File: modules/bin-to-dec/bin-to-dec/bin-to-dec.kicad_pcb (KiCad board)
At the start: 2 copper layers, 78 parts, among them J1 Conn_02x26_Odd_Even, Q100 2N7002, Q101 2N7002, Q102 DMP3099L, Q103 DMP3099L, Q104 2N7002, Q105 2N7002, Q106 2N7002, Q107 DMP3099L, Q108 DMP3099L, Q109 DMP3099L, Q110 DMP3099L, Q111 2N7002, Q112 2N7002, Q113 2N7002, Q114 2N7002, Q115 DMP3099L, Q116 DMP3099L, Q117 DMP3099L, Q118 2N7002, Q119 2N7002, Q120 DMP3099L, Q121 DMP3099L, Q122 2N7002, Q123 2N7002, Q124 2N7002, Q125 DMP3099L, Q126 DMP3099L, Q127 DMP3099L, Q128 2N7002, Q129 2N7002, Q130 2N7002, Q131 DMP3099L, Q132 DMP3099L, Q133 DMP3099L, Q134 2N7002, Q135 2N7002, Q136 DMP3099L, Q137 DMP3099L, Q138 2N7002, Q139 2N7002, Q140 2N7002, Q141 DMP3099L, Q142 DMP3099L, Q143 DMP3099L, Q144 2N7002, Q145 2N7002, Q146 2N7002, Q147 DMP3099L, Q148 DMP3099L, Q75 DMP3099L, Q76 2N7002, Q77 2N7002, Q78 2N7002, Q79 DMP3099L, Q80 DMP3099L, Q81 DMP3099L, Q82 2N7002, Q83 2N7002, Q84 2N7002, Q85 DMP3099L, Q86 DMP3099L, Q87 DMP3099L, Q88 2N7002, Q89 2N7002, Q90 2N7002, Q91 DMP3099L, Q92 DMP3099L, Q93 DMP3099L, Q94 2N7002, Q95 2N7002, Q96 2N7002, Q97 DMP3099L, Q98 DMP3099L, Q99 DMP3099L

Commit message: routed on bdc
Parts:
- added C1: 100n, Capacitor_SMD:C_0603_1608Metric, F.Cu at (250.4, -17.8)
- added C2: 100n, Capacitor_SMD:C_0603_1608Metric, F.Cu at (250.4, -15.3)
- added C3: 100n, Capacitor_SMD:C_0603_1608Metric, F.Cu at (250.4, -12.8)
- added Q1: DMP3099L, Package_TO_SOT_SMD:SOT-23, F.Cu at (253.6, 31.8)
- added Q10: DMP3099L, Package_TO_SOT_SMD:SOT-23, F.Cu at (238.6, -3.65)
- added Q11: DMP3099L, Package_TO_SOT_SMD:SOT-23, F.Cu at (242.8, 31.9)
- added Q12: 2N7002, Package_TO_SOT_SMD:SOT-23, F.Cu at (238.3, 31.9)
- added Q13: 2N7002, Package_TO_SOT_SMD:SOT-23, F.Cu at (238.3, 27.9)
- added Q14: 2N7002, Package_TO_SOT_SMD:SOT-23, F.Cu at (238.3, 35.6)
- added Q15: DMP3099L, Package_TO_SOT_SMD:SOT-23, F.Cu at (242.8, 27.9)
- added Q16: DMP3099L, Package_TO_SOT_SMD:SOT-23, F.Cu at (242.8, 35.6)
- added Q17: DMP3099L, Package_TO_SOT_SMD:SOT-23, F.Cu at (242.6, 18.9)
- added Q18: 2N7002, Package_TO_SOT_SMD:SOT-23, F.Cu at (238.2, 18.9)
- added Q19: 2N7002, Package_TO_SOT_SMD:SOT-23, F.Cu at (238.1, 14.9)
- added Q2: 2N7002, Package_TO_SOT_SMD:SOT-23, F.Cu at (249.1, 31.8)
- added Q20: 2N7002, Package_TO_SOT_SMD:SOT-23, F.Cu at (238.2, 22.6)
- added Q21: DMP3099L, Package_TO_SOT_SMD:SOT-23, F.Cu at (242.6, 14.9)
- added Q22: DMP3099L, Package_TO_SOT_SMD:SOT-23, F.Cu at (242.6, 22.6)
- added Q23: DMP3099L, Package_TO_SOT_SMD:SOT-23, F.Cu at (234.2, -7.83)
- added Q24: 2N7002, Package_TO_SOT_SMD:SOT-23, F.Cu at (234.2, -3.62)
- added Q25: 2N7002, Package_TO_SOT_SMD:SOT-23, F.Cu at (230.4, -7.79)
- added Q26: DMP3099L, Package_TO_SOT_SMD:SOT-23, F.Cu at (230.4, -3.65)
- added Q27: DMP3099L, Package_TO_SOT_SMD:SOT-23, F.Cu at (232.6, 19.0)
- added Q28: 2N7002, Package_TO_SOT_SMD:SOT-23, F.Cu at (228.1, 19.0)
- added Q29: 2N7002, Package_TO_SOT_SMD:SOT-23, F.Cu at (228.1, 15.0)
- added Q3: 2N7002, Package_TO_SOT_SMD:SOT-23, F.Cu at (249.1, 27.9)
- added Q30: 2N7002, Package_TO_SOT_SMD:SOT-23, F.Cu at (228.1, 22.8)
- added Q31: DMP3099L, Package_TO_SOT_SMD:SOT-23, F.Cu at (232.6, 15.0)
- added Q32: DMP3099L, Package_TO_SOT_SMD:SOT-23, F.Cu at (232.6, 22.8)
- added Q33: DMP3099L, Package_TO_SOT_SMD:SOT-23, F.Cu at (232.5, 6.17)
- added Q34: 2N7002, Package_TO_SOT_SMD:SOT-23, F.Cu at (228.0, 6.17)
- added Q35: 2N7002, Package_TO_SOT_SMD:SOT-23, F.Cu at (228.0, 2.20)
- added Q36: 2N7002, Package_TO_SOT_SMD:SOT-23, F.Cu at (228.0, 9.95)
- added Q37: DMP3099L, Package_TO_SOT_SMD:SOT-23, F.Cu at (232.5, 2.20)
- added Q38: DMP3099L, Package_TO_SOT_SMD:SOT-23, F.Cu at (232.5, 9.95)
- added Q39: DMP3099L, Package_TO_SOT_SMD:SOT-23, F.Cu at (241.7, -13.1)
- added Q4: 2N7002, Package_TO_SOT_SMD:SOT-23, F.Cu at (249.2, 35.6)
- added Q40: DMP3099L, Package_TO_SOT_SMD:SOT-23, F.Cu at (245.5, -13.0)
- added Q41: 2N7002, Package_TO_SOT_SMD:SOT-23, F.Cu at (241.7, -17.4)
- added Q42: 2N7002, Package_TO_SOT_SMD:SOT-23, F.Cu at (245.5, -17.4)
- added Q43: 2N7002, Package_TO_SOT_SMD:SOT-23, F.Cu at (237.6, -17.4)
- added Q44: 2N7002, Package_TO_SOT_SMD:SOT-23, F.Cu at (233.6, -17.4)
- added Q45: DMP3099L, Package_TO_SOT_SMD:SOT-23, F.Cu at (237.6, -13.1)
- added Q46: DMP3099L, Package_TO_SOT_SMD:SOT-23, F.Cu at (233.6, -13.1)
- added Q47: DMP3099L, Package_TO_SOT_SMD:SOT-23, F.Cu at (253.5, 18.9)
- added Q48: 2N7002, Package_TO_SOT_SMD:SOT-23, F.Cu at (249.0, 18.9)
- added Q49: 2N7002, Package_TO_SOT_SMD:SOT-23, F.Cu at (249.0, 15.0)
- added Q5: DMP3099L, Package_TO_SOT_SMD:SOT-23, F.Cu at (253.6, 27.9)
- added Q50: 2N7002, Package_TO_SOT_SMD:SOT-23, F.Cu at (249.0, 22.7)
- added Q51: DMP3099L, Package_TO_SOT_SMD:SOT-23, F.Cu at (253.4, 15.0)
- added Q52: DMP3099L, Package_TO_SOT_SMD:SOT-23, F.Cu at (253.5, 22.7)
- added Q53: DMP3099L, Package_TO_SOT_SMD:SOT-23, F.Cu at (253.4, 6.08)
- added Q54: 2N7002, Package_TO_SOT_SMD:SOT-23, F.Cu at (248.9, 6.08)
- added Q55: 2N7002, Package_TO_SOT_SMD:SOT-23, F.Cu at (248.9, 2.10)
- added Q56: 2N7002, Package_TO_SOT_SMD:SOT-23, F.Cu at (248.9, 9.85)
- added Q57: DMP3099L, Package_TO_SOT_SMD:SOT-23, F.Cu at (253.4, 2.10)
- added Q58: DMP3099L, Package_TO_SOT_SMD:SOT-23, F.Cu at (253.4, 9.85)
- added Q59: DMP3099L, Package_TO_SOT_SMD:SOT-23, F.Cu at (250.6, -7.84)
- added Q6: DMP3099L, Package_TO_SOT_SMD:SOT-23, F.Cu at (253.6, 35.6)
- added Q60: 2N7002, Package_TO_SOT_SMD:SOT-23, F.Cu at (250.6, -3.63)
- added Q61: 2N7002, Package_TO_SOT_SMD:SOT-23, F.Cu at (246.7, -7.81)
- added Q62: DMP3099L, Package_TO_SOT_SMD:SOT-23, F.Cu at (246.7, -3.66)
- added Q63: DMP3099L, Package_TO_SOT_SMD:SOT-23, F.Cu at (232.7, 31.8)
- added Q64: 2N7002, Package_TO_SOT_SMD:SOT-23, F.Cu at (228.2, 31.8)
- added Q65: 2N7002, Package_TO_SOT_SMD:SOT-23, F.Cu at (228.2, 27.9)
- added Q66: 2N7002, Package_TO_SOT_SMD:SOT-23, F.Cu at (228.2, 35.6)
- added Q67: DMP3099L, Package_TO_SOT_SMD:SOT-23, F.Cu at (232.6, 27.9)
- added Q68: DMP3099L, Package_TO_SOT_SMD:SOT-23, F.Cu at (232.7, 35.6)
- added Q69: DMP3099L, Package_TO_SOT_SMD:SOT-23, F.Cu at (242.5, 6.03)
- added Q7: DMP3099L, Package_TO_SOT_SMD:SOT-23, F.Cu at (242.4, -7.83)
- added Q70: 2N7002, Package_TO_SOT_SMD:SOT-23, F.Cu at (238.1, 6.03)
- added Q71: 2N7002, Package_TO_SOT_SMD:SOT-23, F.Cu at (238.0, 2.05)
- added Q72: 2N7002, Package_TO_SOT_SMD:SOT-23, F.Cu at (238.1, 9.80)
- added Q73: DMP3099L, Package_TO_SOT_SMD:SOT-23, F.Cu at (242.5, 2.05)
- added Q74: DMP3099L, Package_TO_SOT_SMD:SOT-23, F.Cu at (242.5, 9.80)
- added Q8: 2N7002, Package_TO_SOT_SMD:SOT-23, F.Cu at (242.4, -3.62)
- added Q9: 2N7002, Package_TO_SOT_SMD:SOT-23, F.Cu at (238.6, -7.79)
- moved J1 269.1 mm to (301.3, -48.1)
- moved Q110 164.9 mm to (208.4, -14.6), turned to -90 degrees
- moved Q112 163.4 mm to (208.4, -18.9), turned to -90 degrees
- moved Q109 159.2 mm to (204.6, -14.6), turned to -90 degrees
- moved Q111 157.7 mm to (204.6, -18.9), turned to -90 degrees
- moved Q113 150.6 mm to (200.5, -18.9), turned to -90 degrees
- moved Q114 150.4 mm to (196.5, -18.9), turned to -90 degrees
- moved Q115 144.0 mm to (200.5, -14.6), turned to -90 degrees
- moved Q116 143.8 mm to (196.5, -14.6), turned to -90 degrees
- moved Q131 123.1 mm to (217.4, 2.07)
- moved Q132 121.4 mm to (217.4, 9.82)
- moved Q129 114.7 mm to (212.9, 2.07)
- moved Q130 113.2 mm to (212.9, 9.82)
- moved Q141 113.1 mm to (206.3, 14.9)
- moved Q127 113.1 mm to (217.4, 6.04)
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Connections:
- J1 pad 1: unconnected-(J1-Pin_1-Pad1) -> +3V3
- J1 pad 10: unconnected-(J1-Pin_10-Pad10) -> /BDC1/8
- J1 pad 11: unconnected-(J1-Pin_11-Pad11) -> +3V3
- J1 pad 12: unconnected-(J1-Pin_12-Pad12) -> GND
- J1 pad 13: unconnected-(J1-Pin_13-Pad13) -> /BDC/\Q1
- J1 pad 14: unconnected-(J1-Pin_14-Pad14) -> /BDC1/7
- J1 pad 15: unconnected-(J1-Pin_15-Pad15) -> /BDC/Q1
- J1 pad 16: unconnected-(J1-Pin_16-Pad16) -> /BDC1/6
- J1 pad 17: unconnected-(J1-Pin_17-Pad17) -> /BDC/\Q0
- J1 pad 18: unconnected-(J1-Pin_18-Pad18) -> /BDC1/5
- J1 pad 19: unconnected-(J1-Pin_19-Pad19) -> /BDC/Q0
- J1 pad 2: unconnected-(J1-Pin_2-Pad2) -> GND
- J1 pad 20: unconnected-(J1-Pin_20-Pad20) -> /BDC1/4
- J1 pad 21: unconnected-(J1-Pin_21-Pad21) -> +3V3
- J1 pad 22: unconnected-(J1-Pin_22-Pad22) -> GND
- J1 pad 23: unconnected-(J1-Pin_23-Pad23) -> /BDC/0
- J1 pad 24: unconnected-(J1-Pin_24-Pad24) -> /BDC1/3
- J1 pad 25: unconnected-(J1-Pin_25-Pad25) -> /BDC/1
- J1 pad 26: unconnected-(J1-Pin_26-Pad26) -> /BDC1/2
- J1 pad 27: unconnected-(J1-Pin_27-Pad27) -> /BDC/2
- J1 pad 28: unconnected-(J1-Pin_28-Pad28) -> /BDC1/1
- J1 pad 29: unconnected-(J1-Pin_29-Pad29) -> /BDC/3
- J1 pad 3: unconnected-(J1-Pin_3-Pad3) -> /BDC/\Q3
- J1 pad 30: unconnected-(J1-Pin_30-Pad30) -> /BDC1/0
- J1 pad 31: unconnected-(J1-Pin_31-Pad31) -> +3V3
- J1 pad 32: unconnected-(J1-Pin_32-Pad32) -> GND
- J1 pad 33: unconnected-(J1-Pin_33-Pad33) -> /BDC/4
- J1 pad 34: unconnected-(J1-Pin_34-Pad34) -> /BDC1/Q0
- J1 pad 35: unconnected-(J1-Pin_35-Pad35) -> /BDC/5
- J1 pad 36: unconnected-(J1-Pin_36-Pad36) -> /BDC1/\Q0
- J1 pad 37: unconnected-(J1-Pin_37-Pad37) -> /BDC/6
- J1 pad 38: unconnected-(J1-Pin_38-Pad38) -> /BDC1/Q1
- J1 pad 39: unconnected-(J1-Pin_39-Pad39) -> /BDC/7
- J1 pad 40: unconnected-(J1-Pin_40-Pad40) -> /BDC1/\Q1
- J1 pad 41: unconnected-(J1-Pin_41-Pad41) -> +3V3
- J1 pad 42: unconnected-(J1-Pin_42-Pad42) -> GND
- J1 pad 43: unconnected-(J1-Pin_43-Pad43) -> /BDC/8
- J1 pad 44: unconnected-(J1-Pin_44-Pad44) -> /BDC1/Q2
- J1 pad 45: unconnected-(J1-Pin_45-Pad45) -> /BDC/9
- J1 pad 46: unconnected-(J1-Pin_46-Pad46) -> /BDC1/\Q2
- J1 pad 47: unconnected-(J1-Pin_47-Pad47) -> +3V3
- J1 pad 48: unconnected-(J1-Pin_48-Pad48) -> /BDC1/Q3
- J1 pad 5: unconnected-(J1-Pin_5-Pad5) -> /BDC/Q3
- J1 pad 50: unconnected-(J1-Pin_50-Pad50) -> /BDC1/\Q3
- J1 pad 52: unconnected-(J1-Pin_52-Pad52) -> GND
- J1 pad 6: unconnected-(J1-Pin_6-Pad6) -> GND
- J1 pad 7: unconnected-(J1-Pin_7-Pad7) -> /BDC/\Q2
- J1 pad 8: unconnected-(J1-Pin_8-Pad8) -> /BDC1/9
- J1 pad 9: unconnected-(J1-Pin_9-Pad9) -> /BDC/Q2
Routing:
- net /BDC1/\Q1: track 0.00 -> 135.0 mm, vias 0 -> 9
- net /BDC1/Q0: track 0.00 -> 114.0 mm, vias 0 -> 10
- net +3V3: track 0.00 -> 112.3 mm, vias 0 -> 74
- net /BDC1/\Q0: track 0.00 -> 107.5 mm, vias 0 -> 10
- net /BDC1/Q1: track 0.00 -> 103.2 mm, vias 0 -> 7
- net /BDC1/5: track 0.00 -> 101.0 mm, vias 0 -> 2
- net /BDC1/6: track 0.00 -> 77.0 mm
- net /BDC1/nand5/Out: track 0.00 -> 75.3 mm, vias 0 -> 5
- net /BDC1/\Q2: track 0.00 -> 71.3 mm, vias 0 -> 3
- net /BDC1/9: track 0.00 -> 69.3 mm
- net /BDC1/4: track 0.00 -> 68.6 mm
- net /BDC1/\Q3: track 0.00 -> 63.3 mm, vias 0 -> 3
- net /BDC1/Q3: track 0.00 -> 63.3 mm, vias 0 -> 1
- net /BDC1/nand1/Out: track 0.00 -> 61.2 mm, vias 0 -> 4
- net /BDC1/8: track 0.00 -> 55.9 mm
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
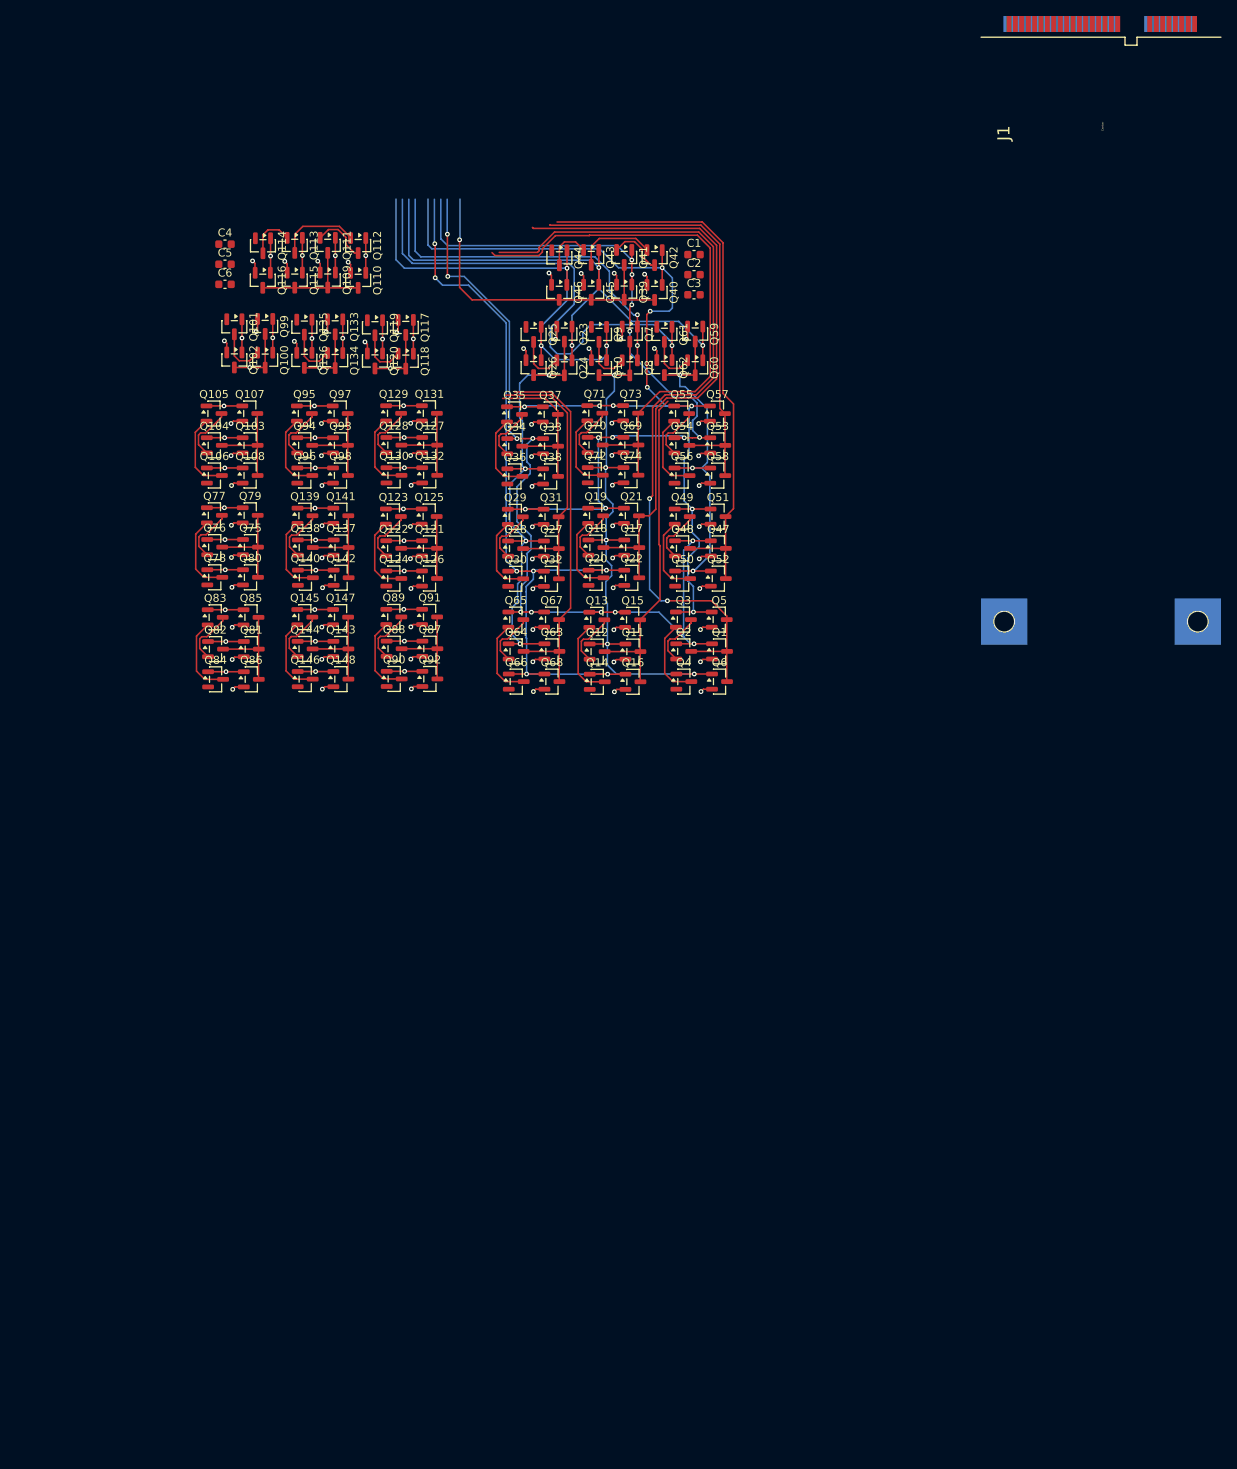
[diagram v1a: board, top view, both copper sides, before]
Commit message: went from routed bin-to-dec to gate only
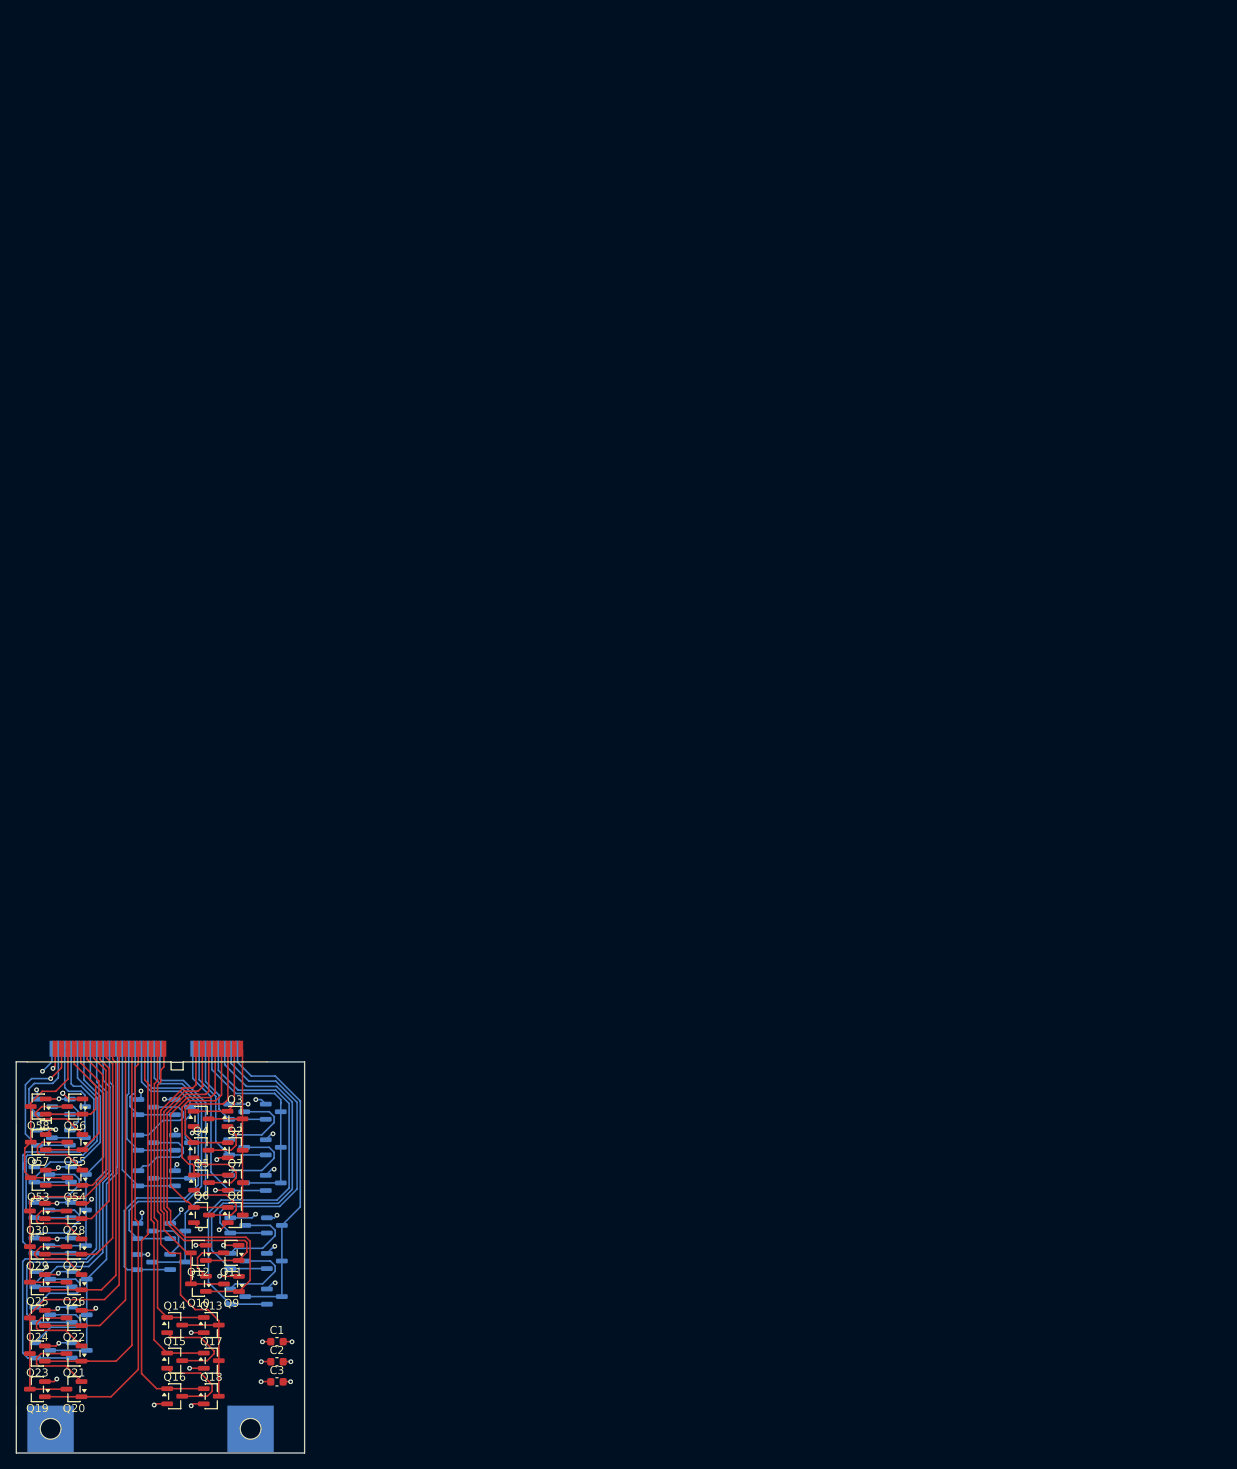
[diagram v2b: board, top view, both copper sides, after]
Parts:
- removed C4, C5, C6: 100n, Capacitor_SMD:C_0603_1608Metric
- removed Q100, Q101, Q104, Q105, Q106, Q111, Q112, Q113, Q114, Q118, Q119, Q122, Q123, Q124, Q128, Q129, Q130, Q134, Q135, Q138, Q139, Q140, Q144, Q145, Q146, Q76, Q77, Q78, Q82, Q83, Q84, Q88, Q89, Q90, Q94, Q95, Q96: 2N7002, Package_TO_SOT_SMD:SOT-23
- removed Q102, Q103, Q107, Q108, Q109, Q110, Q115, Q116, Q117, Q120, Q121, Q125, Q126, Q127, Q131, Q132, Q133, Q136, Q137, Q141, Q142, Q143, Q147, Q148, Q75, Q79, Q80, Q81, Q85, Q86, Q87, Q91, Q92, Q93, Q97, Q98, Q99: DMP3099L, Package_TO_SOT_SMD:SOT-23
- Q10, Q11, Q15, Q16, Q21, Q22, Q26, Q27, Q5, Q6: value DMP3099L -> 2N7002
- Q12, Q13, Q18, Q19, Q2, Q24, Q25, Q29, Q30, Q8, Q9: value 2N7002 -> DMP3099L
- Q31, Q36, Q39, Q40, Q42, Q43, Q44, Q45, Q46, Q47, Q48, Q49, Q50, Q51, Q52, Q59, Q60, Q61, Q62, Q63, Q64, Q65, Q66, Q67, Q68, Q69, Q70, Q71, Q72, Q73, Q74: moved to B.Cu
- Q32, Q33, Q37, Q38: value DMP3099L -> 2N7002; moved to B.Cu
- Q34, Q35, Q41: value 2N7002 -> DMP3099L; moved to B.Cu
- moved J1 175.0 mm to (182.1, 79.9)
- moved Q42 156.6 mm to (169.0, 119.2), turned to 0 degrees
- moved Q41 152.7 mm to (173.6, 119.2), turned to 0 degrees
- moved Q43 148.9 mm to (169.0, 114.7), turned to 0 degrees
- moved C1 145.5 mm to (198.3, 118.1)
- moved C2 145.5 mm to (198.3, 120.6)
- moved C3 145.5 mm to (198.3, 123.1)
- moved Q23 143.4 mm to (168.3, 119.6), turned to 180 degrees
- moved Q44 143.1 mm to (169.0, 110.3), turned to 0 degrees
- moved Q45 142.9 mm to (173.6, 114.7), turned to 0 degrees
- moved Q46 137.2 mm to (173.6, 110.3), turned to 0 degrees
- moved Q24 135.8 mm to (168.3, 115.1), turned to 180 degrees
- moved Q59 134.9 mm to (181.8, 108.2), turned to 0 degrees
- moved Q25 133.7 mm to (168.4, 110.7), turned to 180 degrees
- moved Q39 133.5 mm to (173.5, 101.7), turned to 0 degrees
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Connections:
- J1 pad 1: +3V3 -> /nand4_out
- J1 pad 10: /BDC1/8 -> /nand3_8_out
- J1 pad 11: +3V3 -> /nand2_1_A
- J1 pad 12: GND -> /nand3_8_C
- J1 pad 13: /BDC/\Q1 -> /nand2_1_B
- J1 pad 14: /BDC1/7 -> /nand3_8_B
- J1 pad 15: /BDC/Q1 -> /nand2_1_out
- J1 pad 16: /BDC1/6 -> /nand3_8_A
- J1 pad 17: /BDC/\Q0 -> /nand3_1_out
- J1 pad 18: /BDC1/5 -> /nand2_3_out
- J1 pad 19: /BDC/Q0 -> /nand3_1_A
- J1 pad 2: GND -> /nand3_9_out
- J1 pad 20: /BDC1/4 -> /nand2_3_B
- J1 pad 21: +3V3 -> /nand3_1_B
- J1 pad 22: GND -> /nand2_3_A
- J1 pad 23: /BDC/0 -> /nand3_1_C
- J1 pad 24: /BDC1/3 -> /nand3_7_out
- J1 pad 25: /BDC/1 -> /nand3_2_A
- J1 pad 26: /BDC1/2 -> /nand3_7_C
- J1 pad 27: /BDC/2 -> /nand3_2_B
- J1 pad 28: /BDC1/1 -> /nand3_7_B
- J1 pad 29: /BDC/3 -> /nand3_2_C
- J1 pad 3: /BDC/\Q3 -> /nand4_A
- J1 pad 30: /BDC1/0 -> /nand3_7_A
- J1 pad 31: +3V3 -> /nand3_2_out
- J1 pad 32: GND -> /nand3_6_out
- J1 pad 33: /BDC/4 -> /nand3_3_A
- J1 pad 34: /BDC1/Q0 -> /nand3_6_C
- J1 pad 35: /BDC/5 -> /nand3_3_B
- J1 pad 36: /BDC1/\Q0 -> /nand3_6_B
- J1 pad 37: /BDC/6 -> /nand3_3_C
- J1 pad 38: /BDC1/Q1 -> /nand3_6_A
- J1 pad 39: /BDC/7 -> /nand3_3_out
- J1 pad 4: unconnected-(J1-Pin_4-Pad4) -> /nand3_9_C
- J1 pad 40: /BDC1/\Q1 -> /nand3_5_out
- J1 pad 41: +3V3 -> /nand3_4_A
- J1 pad 42: GND -> /nand3_5_C
- J1 pad 43: /BDC/8 -> /nand3_4_B
- J1 pad 44: /BDC1/Q2 -> /nand3_5_B
- J1 pad 45: /BDC/9 -> /nand3_4_C
- J1 pad 46: /BDC1/\Q2 -> /nand3_5_A
- J1 pad 47: +3V3 -> /nand3_4_out
- J1 pad 48: /BDC1/Q3 -> /nand2_2_out
- J1 pad 49: unconnected-(J1-Pin_49-Pad49) -> /nand2_2_A
- J1 pad 5: /BDC/Q3 -> /nand4_B
- J1 pad 50: /BDC1/\Q3 -> /nand2_2_B
- J1 pad 51: unconnected-(J1-Pin_51-Pad51) -> GND
- J1 pad 52: GND -> +3V3
- J1 pad 6: GND -> /nand3_9_B
- J1 pad 7: /BDC/\Q2 -> /nand4_C
- J1 pad 8: /BDC1/9 -> /nand3_9_A
- J1 pad 9: /BDC/Q2 -> /nand4_D
- Q1 pad 1: /BDC1/Q0 -> /nand4_A
- Q1 pad 3: /BDC1/5 -> /nand4_out
- Q10 pad 1: /BDC1/\Q3 -> /nand2_1_A
- Q10 pad 2: +3V3 -> Net-(Q10-S)
- Q10 pad 3: /BDC1/nand5/Out -> /nand2_1_out
- Q11 pad 1: /BDC1/nand5/Out -> /nand2_1_B
- Q11 pad 2: +3V3 -> GND
- Q11 pad 3: /BDC1/7 -> Net-(Q10-S)
- Q12 pad 1: /BDC1/nand5/Out -> /nand2_1_B
- Q12 pad 2: Net-(Q12-S) -> +3V3
- Q12 pad 3: /BDC1/7 -> /nand2_1_out
- Q13 pad 1: /BDC1/Q0 -> /nand3_1_A
- Q13 pad 2: Net-(Q13-S) -> +3V3
- Q13 pad 3: Net-(Q12-S) -> /nand3_1_out
- Q14 pad 1: /BDC1/Q1 -> /nand3_1_A
- Q14 pad 2: GND -> Net-(Q14-S)
- Q14 pad 3: Net-(Q13-S) -> /nand3_1_out
- Q15 pad 1: /BDC1/Q0 -> /nand3_1_B
- Q15 pad 2: +3V3 -> Net-(Q15-S)
- Q15 pad 3: /BDC1/7 -> Net-(Q14-S)
- Q16 pad 1: /BDC1/Q1 -> /nand3_1_C
- Q16 pad 2: +3V3 -> GND
- Q16 pad 3: /BDC1/7 -> Net-(Q15-S)
- Q17 pad 1: /BDC1/nand5/Out -> /nand3_1_B
- Q17 pad 3: /BDC1/6 -> /nand3_1_out
- Q18 pad 1: /BDC1/nand5/Out -> /nand3_1_C
- Q18 pad 2: Net-(Q18-S) -> +3V3
- Q18 pad 3: /BDC1/6 -> /nand3_1_out
- Q19 pad 1: /BDC1/\Q0 -> /nand3_2_A
- Q19 pad 2: Net-(Q19-S) -> +3V3
- Q19 pad 3: Net-(Q18-S) -> /nand3_2_out
- Q2 pad 1: /BDC1/Q0 -> /nand4_B
- Q2 pad 2: Net-(Q2-S) -> +3V3
- Q2 pad 3: /BDC1/5 -> /nand4_out
- Q20 pad 1: /BDC1/Q1 -> /nand3_2_A
- Q20 pad 2: GND -> Net-(Q20-S)
- Q20 pad 3: Net-(Q19-S) -> /nand3_2_out
- Q21 pad 1: /BDC1/\Q0 -> /nand3_2_B
- Q21 pad 2: +3V3 -> Net-(Q21-S)
- Q21 pad 3: /BDC1/6 -> Net-(Q20-S)
- Q22 pad 1: /BDC1/Q1 -> /nand3_2_C
- Q22 pad 2: +3V3 -> GND
- Q22 pad 3: /BDC1/6 -> Net-(Q21-S)
- Q23 pad 1: /BDC1/\Q2 -> /nand3_2_B
- Q23 pad 3: /BDC1/nand1/Out -> /nand3_2_out
- Q24 pad 1: /BDC1/\Q2 -> /nand3_2_C
- Q24 pad 2: Net-(Q24-S) -> +3V3
- Q24 pad 3: /BDC1/nand1/Out -> /nand3_2_out
- Q25 pad 1: /BDC1/\Q3 -> /nand3_3_A
- Q25 pad 2: GND -> +3V3
- Q25 pad 3: Net-(Q24-S) -> /nand3_3_out
- Q26 pad 1: /BDC1/\Q3 -> /nand3_3_A
- Q26 pad 2: +3V3 -> Net-(Q26-S)
- Q26 pad 3: /BDC1/nand1/Out -> /nand3_3_out
- Q27 pad 1: /BDC1/nand1/Out -> /nand3_3_B
- Q27 pad 2: +3V3 -> Net-(Q27-S)
- Q27 pad 3: /BDC1/2 -> Net-(Q26-S)
- Q28 pad 1: /BDC1/nand1/Out -> /nand3_3_C
- Q28 pad 2: Net-(Q28-S) -> GND
- Q28 pad 3: /BDC1/2 -> Net-(Q27-S)
- Q29 pad 1: /BDC1/\Q0 -> /nand3_3_B
- Q29 pad 2: Net-(Q29-S) -> +3V3
- Q29 pad 3: Net-(Q28-S) -> /nand3_3_out
- Q3 pad 1: /BDC1/\Q1 -> /nand4_A
- Q3 pad 3: Net-(Q2-S) -> /nand4_out
- Q30 pad 1: /BDC1/Q1 -> /nand3_3_C
- Q30 pad 2: GND -> +3V3
- Q30 pad 3: Net-(Q29-S) -> /nand3_3_out
- Q31 pad 1: /BDC1/\Q0 -> /nand2_2_A
- Q31 pad 3: /BDC1/2 -> /nand2_2_out
- Q32 pad 1: /BDC1/Q1 -> /nand2_2_A
- Q32 pad 2: +3V3 -> Net-(Q32-S)
- Q32 pad 3: /BDC1/2 -> /nand2_2_out
- Q33 pad 1: /BDC1/Q0 -> /nand2_2_B
- Q33 pad 2: +3V3 -> GND
- Q33 pad 3: /BDC1/1 -> Net-(Q32-S)
- Q34 pad 1: /BDC1/Q0 -> /nand2_2_B
- Q34 pad 2: Net-(Q34-S) -> +3V3
- Q34 pad 3: /BDC1/1 -> /nand2_2_out
- Q35 pad 1: /BDC1/\Q1 -> /nand3_5_A
- Q35 pad 2: Net-(Q35-S) -> +3V3
- Q35 pad 3: Net-(Q34-S) -> /nand3_5_out
- Q36 pad 1: /BDC1/nand1/Out -> /nand3_5_A
- Q36 pad 2: GND -> Net-(Q36-S)
- Q36 pad 3: Net-(Q35-S) -> /nand3_5_out
- Q37 pad 1: /BDC1/\Q1 -> /nand3_5_B
- Q37 pad 2: +3V3 -> Net-(Q37-S)
- Q37 pad 3: /BDC1/1 -> Net-(Q36-S)
- Q38 pad 1: /BDC1/nand1/Out -> /nand3_5_C
- Q38 pad 2: +3V3 -> GND
- Q38 pad 3: /BDC1/1 -> Net-(Q37-S)
- Q39 pad 1: /BDC1/\Q0 -> /nand3_5_B
- Q39 pad 3: /BDC1/0 -> /nand3_5_out
- Q4 pad 1: /BDC1/nand5/Out -> /nand4_B
- Q4 pad 2: GND -> Net-(Q4-S)
- Q40 pad 1: /BDC1/\Q1 -> /nand3_5_C
- Q40 pad 3: /BDC1/0 -> /nand3_5_out
- Q41 pad 1: /BDC1/\Q0 -> /nand3_6_A
- Q41 pad 2: Net-(Q41-S) -> +3V3
- Q41 pad 3: /BDC1/0 -> /nand3_6_out
- Q42 pad 1: /BDC1/\Q1 -> /nand3_6_A
- Q42 pad 3: Net-(Q41-S) -> /nand3_6_out
- Q43 pad 1: /BDC1/\Q2 -> /nand3_6_B
- Q44 pad 1: /BDC1/\Q3 -> /nand3_6_C
- Q45 pad 1: /BDC1/\Q2 -> /nand3_6_B
- Q45 pad 3: /BDC1/0 -> /nand3_6_out
- Q46 pad 1: /BDC1/\Q3 -> /nand3_6_C
- Q46 pad 3: /BDC1/0 -> /nand3_6_out
- Q47 pad 1: /BDC1/Q0 -> /nand3_7_A
- Q47 pad 3: /BDC1/9 -> /nand3_7_out
- Q48 pad 1: /BDC1/Q0 -> /nand3_7_A
- Q48 pad 3: /BDC1/9 -> /nand3_7_out
- Q49 pad 1: /BDC1/\Q1 -> /nand3_7_B
- Q5 pad 1: /BDC1/\Q1 -> /nand4_C
- Q5 pad 2: +3V3 -> Net-(Q5-S)
- Q5 pad 3: /BDC1/5 -> Net-(Q4-S)
- Q50 pad 1: /BDC1/nand10/Out -> /nand3_7_C
- Q51 pad 1: /BDC1/\Q1 -> /nand3_7_B
- Q51 pad 3: /BDC1/9 -> /nand3_7_out
- Q52 pad 1: /BDC1/nand10/Out -> /nand3_7_C
- Q52 pad 3: /BDC1/9 -> /nand3_7_out
- Q53 pad 1: /BDC1/\Q0 -> /nand3_4_A
- Q53 pad 3: /BDC1/8 -> /nand3_4_out
- Q54 pad 1: /BDC1/\Q0 -> /nand3_4_A
- Q54 pad 3: /BDC1/8 -> /nand3_4_out
- Q55 pad 1: /BDC1/\Q1 -> /nand3_4_B
- Q56 pad 1: /BDC1/nand10/Out -> /nand3_4_C
- Q57 pad 1: /BDC1/\Q1 -> /nand3_4_B
- Q57 pad 3: /BDC1/8 -> /nand3_4_out
- Q58 pad 1: /BDC1/nand10/Out -> /nand3_4_C
- Q58 pad 3: /BDC1/8 -> /nand3_4_out
- Q59 pad 1: /BDC1/\Q2 -> /nand2_3_A
- Q59 pad 3: /BDC1/nand10/Out -> /nand2_3_out
- Q6 pad 1: /BDC1/nand5/Out -> /nand4_D
- Q6 pad 2: +3V3 -> GND
- Q6 pad 3: /BDC1/5 -> Net-(Q5-S)
- Q60 pad 1: /BDC1/\Q2 -> /nand2_3_A
- Q60 pad 3: /BDC1/nand10/Out -> /nand2_3_out
- Q61 pad 1: /BDC1/Q3 -> /nand2_3_B
- Q62 pad 1: /BDC1/Q3 -> /nand2_3_B
- Q62 pad 3: /BDC1/nand10/Out -> /nand2_3_out
- Q63 pad 1: /BDC1/nand1/Out -> /nand3_9_A
- Q63 pad 3: /BDC1/3 -> /nand3_9_out
- Q64 pad 1: /BDC1/nand1/Out -> /nand3_9_A
- Q64 pad 3: /BDC1/3 -> /nand3_9_out
- Q65 pad 1: /BDC1/Q0 -> /nand3_9_B
- Q66 pad 1: /BDC1/Q1 -> /nand3_9_C
- Q67 pad 1: /BDC1/Q0 -> /nand3_9_B
- Q67 pad 3: /BDC1/3 -> /nand3_9_out
- Q68 pad 1: /BDC1/Q1 -> /nand3_9_C
- Q68 pad 3: /BDC1/3 -> /nand3_9_out
- Q69 pad 1: /BDC1/\Q0 -> /nand3_8_A
- Q69 pad 3: /BDC1/4 -> /nand3_8_out
- Q7 pad 1: /BDC1/Q2 -> /nand4_C
- Q7 pad 3: /BDC1/nand5/Out -> /nand4_out
- Q70 pad 1: /BDC1/\Q0 -> /nand3_8_A
- Q70 pad 3: /BDC1/4 -> /nand3_8_out
- Q71 pad 1: /BDC1/\Q1 -> /nand3_8_B
- Q72 pad 1: /BDC1/nand5/Out -> /nand3_8_C
- Q73 pad 1: /BDC1/\Q1 -> /nand3_8_B
- Q73 pad 3: /BDC1/4 -> /nand3_8_out
- Q74 pad 1: /BDC1/nand5/Out -> /nand3_8_C
- Q74 pad 3: /BDC1/4 -> /nand3_8_out
- Q8 pad 1: /BDC1/Q2 -> /nand4_D
- Q8 pad 2: Net-(Q8-S) -> +3V3
- Q8 pad 3: /BDC1/nand5/Out -> /nand4_out
- Q9 pad 1: /BDC1/\Q3 -> /nand2_1_A
- Q9 pad 2: GND -> +3V3
- Q9 pad 3: Net-(Q8-S) -> /nand2_1_out
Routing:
- net /BDC1/\Q1: track 135.0 -> 0.00 mm, vias 9 -> 0
- net /BDC1/Q0: track 114.0 -> 0.00 mm, vias 10 -> 0
- net /BDC1/\Q0: track 107.5 -> 0.00 mm, vias 10 -> 0
- net /BDC1/Q1: track 103.2 -> 0.00 mm, vias 7 -> 0
- net /BDC1/5: track 101.0 -> 0.00 mm, vias 2 -> 0
- net /BDC1/6: track 77.0 -> 0.00 mm
- net /BDC1/nand5/Out: track 75.3 -> 0.00 mm, vias 5 -> 0
- net /BDC1/\Q2: track 71.3 -> 0.00 mm, vias 3 -> 0
- net /BDC1/9: track 69.3 -> 0.00 mm
- net /BDC1/4: track 68.6 -> 0.00 mm
- net /BDC1/\Q3: track 63.3 -> 0.00 mm, vias 3 -> 0
- net /BDC1/Q3: track 63.3 -> 0.00 mm, vias 1 -> 0
- net /BDC1/nand1/Out: track 61.2 -> 0.00 mm, vias 4 -> 0
- net /nand3_2_out: track 0.00 -> 56.1 mm
- net /BDC1/8: track 55.9 -> 0.00 mm
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- added copper zone on In1.Cu, net +3V3
- added copper zone on In2.Cu, net GND
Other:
- board outline added: 36.1 x 48.9 mm
- copper layers 2 -> 4
